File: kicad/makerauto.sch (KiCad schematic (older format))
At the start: 15 parts, among them P1 Logo_MA, P2 Mirror, P3 Mirror, P4 Pin, P5 Pin, P6 Pin, P7 Pin

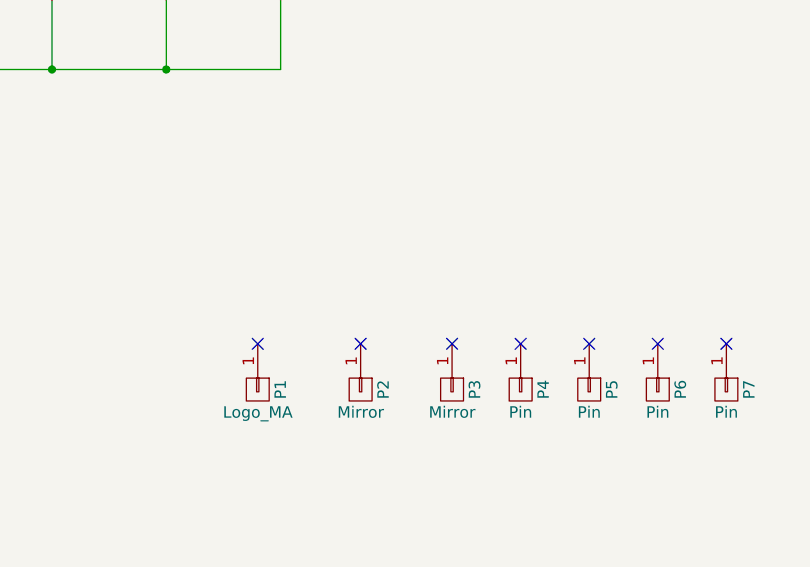
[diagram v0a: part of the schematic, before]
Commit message: added copper fill zones
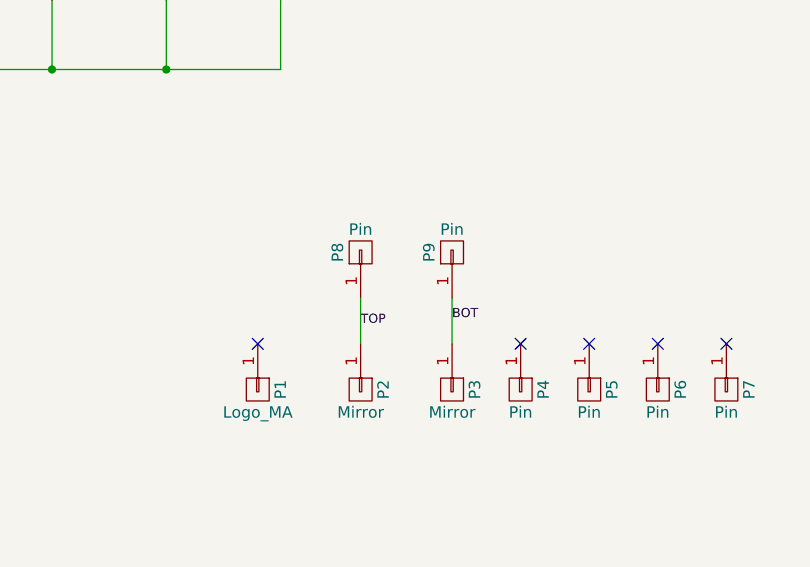
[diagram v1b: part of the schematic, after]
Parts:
- added P8, P9: Pin, makerauto:MTG_0mm8, symbol CONN_01X01
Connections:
- net TOP: now reaches P2.1 (P1)
- net TOP: now also P8.1 (P1)
- net BOT: now reaches P3.1 (P1)
- net BOT: now also P9.1 (P1)
- no-connect marks 7 -> 5
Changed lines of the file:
@@
 	0    1    1    0
 $EndComp
-NoConn ~ 7650 5850
 Text Label 5025 2675 0    50   ~ 10
 3V
@@
 	0    1    1    0
 $EndComp
-NoConn ~ 8050 5850
 $Comp
 L CONN_01X01 P4
@@
 $EndComp
 NoConn ~ 9250 5850
+Wire Wire Line
+	7650 5850 7650 5650
+Wire Wire Line
+	8050 5850 8050 5650
+Text Label 7650 5775 0    40   ~ 0
+TOP
+Text Label 8050 5750 0    40   ~ 0
+BOT
+$Comp
+L CONN_01X01 P8
+U 1 1 57AD6867
+P 7650 5450
+F 0 "P8" H 7650 5550 50  0000 C CNN
+F 1 "Pin" V 7750 5450 50  0000 C CNN
+F 2 "makerauto:MTG_0mm8" H 7650 5450 50  0001 C CNN
+F 3 "" H 7650 5450 50  0000 C CNN
+	1    7650 5450
+	0    -1   -1   0
+$EndComp
+$Comp
+L CONN_01X01 P9
+U 1 1 57AD6923
+P 8050 5450
+F 0 "P9" H 8050 5550 50  0000 C CNN
+F 1 "Pin" V 8150 5450 50  0000 C CNN
+F 2 "makerauto:MTG_0mm8" H 8050 5450 50  0001 C CNN
+F 3 "" H 8050 5450 50  0000 C CNN
+	1    8050 5450
+	0    -1   -1   0
+$EndComp
 $EndSCHEMATC
